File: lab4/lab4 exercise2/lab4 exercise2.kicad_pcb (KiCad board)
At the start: 2 copper layers, 10 parts, among them J1 Conn_01x02_Male, U1 NE555D

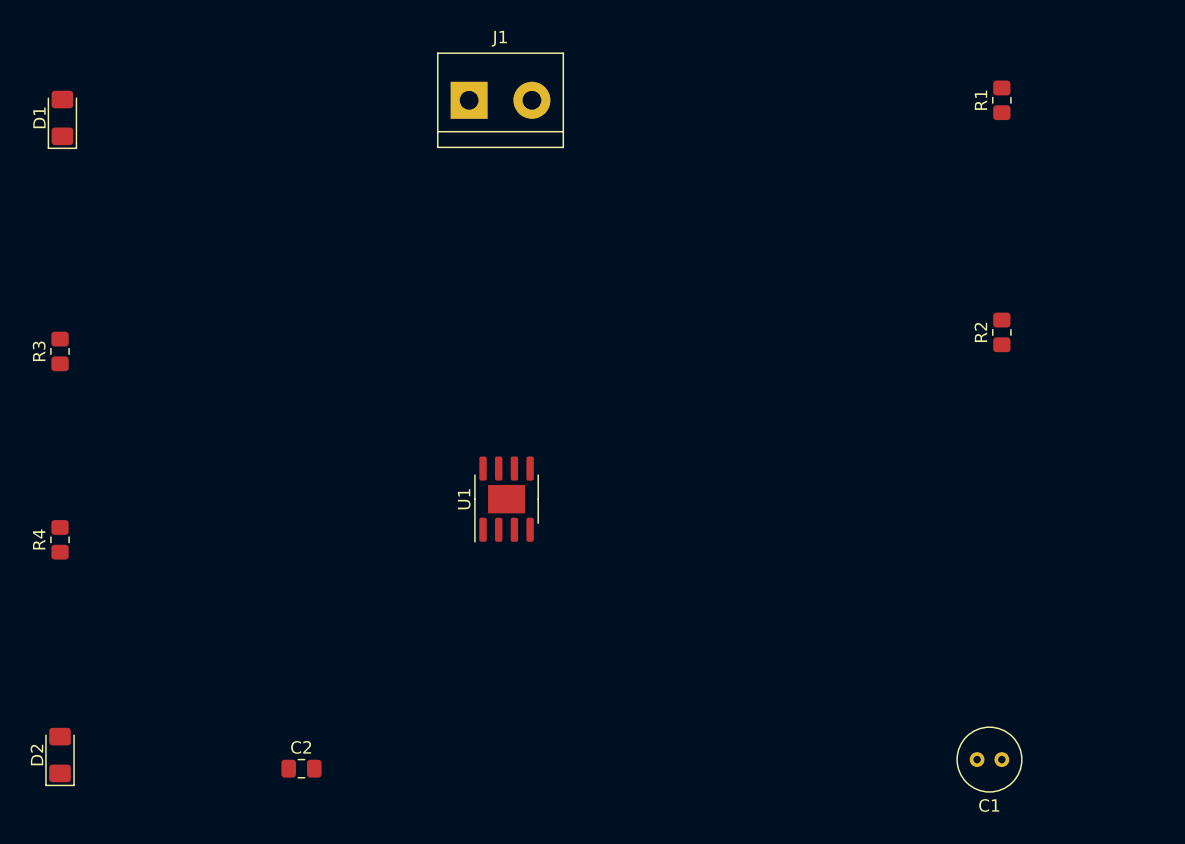
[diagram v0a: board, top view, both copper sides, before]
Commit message: Updated lab 4 pcb layout
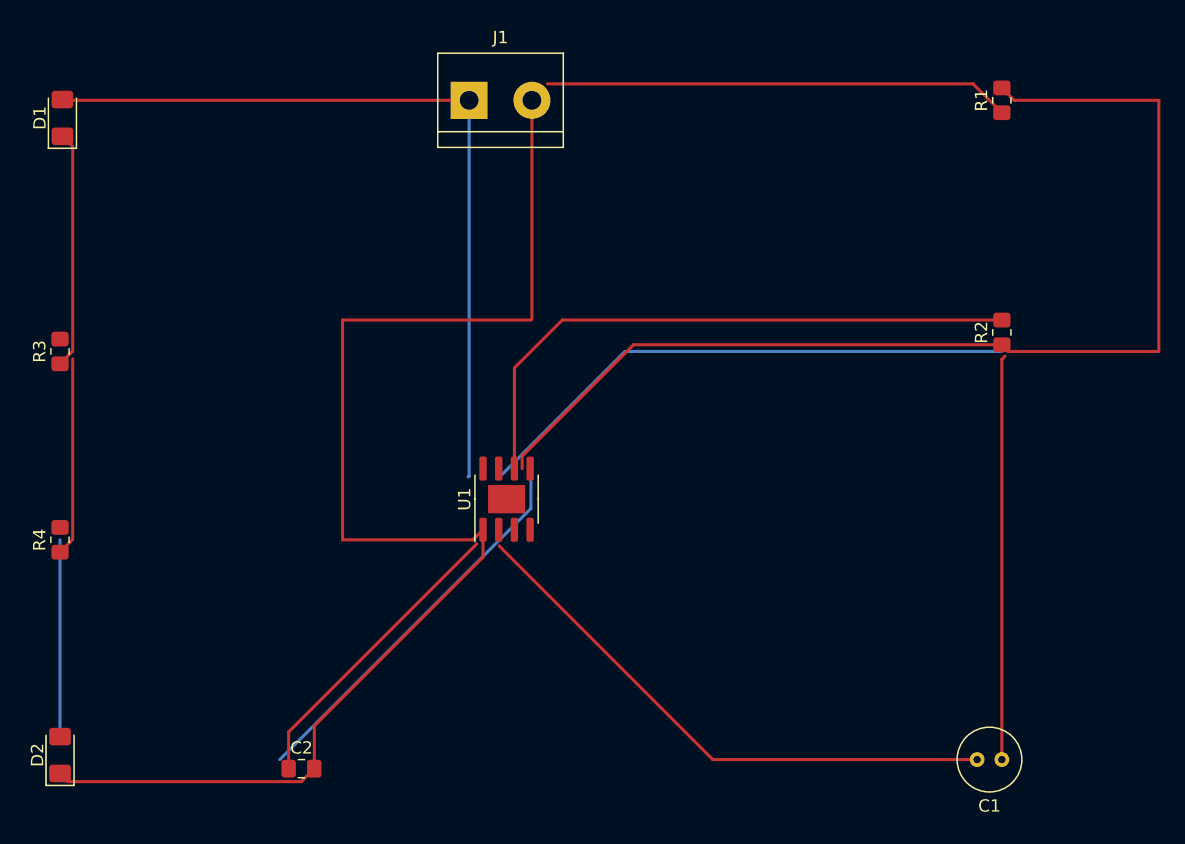
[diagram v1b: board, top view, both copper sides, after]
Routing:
- net GND: track 0.00 -> 154.5 mm
- net +9V: track 0.00 -> 101.2 mm
- net (no net): track 0.00 -> 91.4 mm
- net Net-(R1-Pad2): track 0.00 -> 90.4 mm
- net Net-(C1-Pad1): track 0.00 -> 81.9 mm
- net Net-(C2-Pad1): track 0.00 -> 24.5 mm
- net Net-(D1-Pad1): track 0.00 -> 19.2 mm
- net Net-(R3-Pad2): track 0.00 -> 16.1 mm
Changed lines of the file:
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@@
     )
   )
+  (segment (start 124.46 101.6) (end 104.14 121.92) (width 0.25) (layer "B.Cu") (net 0))
+  (segment (start 86.36 119.38) (end 86.36 104.14) (width 0.25) (layer "B.Cu") (net 0))
+  (segment (start 162.56 88.9) (end 132.08 88.9) (width 0.25) (layer "B.Cu") (net 0))
+  (segment (start 124.46 99.06) (end 124.46 101.6) (width 0.25) (layer "B.Cu") (net 0))
+  (segment (start 132.08 88.9) (end 121.92 99.06) (width 0.25) (layer "B.Cu") (net 0))
+  (segment (start 127 86.36) (end 123.125 90.235) (width 0.25) (layer "F.Cu") (net 1))
+  (segment (start 162.56 89.536396) (end 162.811396 89.285) (width 0.25) (layer "F.Cu") (net 1))
+  (segment (start 162.56 86.36) (end 127 86.36) (width 0.25) (layer "F.Cu") (net 1))
+  (segment (start 162.56 121.92) (end 162.56 89.536396) (width 0.25) (layer "F.Cu") (net 1))
+  (segment (start 123.125 90.235) (end 123.125 98.375) (width 0.25) (layer "F.Cu") (net 1))
+  (segment (start 109.22 86.36) (end 109.22 104.14) (width 0.25) (layer "F.Cu") (net 2))
+  (segment (start 124.54 68.58) (end 124.54 86.28) (width 0.25) (layer "F.Cu") (net 2))
+  (segment (start 105.883744 123.705) (end 106.933744 122.655) (width 0.25) (layer "F.Cu") (net 2))
+  (segment (start 109.22 104.14) (end 119.77 104.14) (width 0.25) (layer "F.Cu") (net 2))
+  (segment (start 120.585 105.548249) (end 120.585 103.325) (width 0.25) (layer "F.Cu") (net 2))
+  (segment (start 106.933744 119.199505) (end 120.585 105.548249) (width 0.25) (layer "F.Cu") (net 2))
+  (segment (start 87.0275 123.705) (end 105.883744 123.705) (width 0.25) (layer "F.Cu") (net 2))
+  (segment (start 160.56 121.92) (end 139.18 121.92) (width 0.25) (layer "F.Cu") (net 2))
+  (segment (start 139.18 121.92) (end 121.885 104.625) (width 0.25) (layer "F.Cu") (net 2))
+  (segment (start 106.933744 122.655) (end 106.933744 119.199505) (width 0.25) (layer "F.Cu") (net 2))
+  (segment (start 119.77 104.14) (end 120.585 103.325) (width 0.25) (layer "F.Cu") (net 2))
+  (segment (start 86.36 123.0375) (end 87.0275 123.705) (width 0.25) (layer "F.Cu") (net 2))
+  (segment (start 124.46 86.36) (end 109.22 86.36) (width 0.25) (layer "F.Cu") (net 2))
+  (segment (start 104.858744 119.687652) (end 120.079823 104.466573) (width 0.25) (layer "F.Cu") (net 3))
+  (segment (start 104.858744 122.655) (end 104.858744 119.687652) (width 0.25) (layer "F.Cu") (net 3))
+  (segment (start 87.385 88.875) (end 86.36 89.9) (width 0.25) (layer "F.Cu") (net 4))
+  (segment (start 86.555 71.4925) (end 87.385 72.3225) (width 0.25) (layer "F.Cu") (net 4))
+  (segment (start 87.385 72.3225) (end 87.385 88.875) (width 0.25) (layer "F.Cu") (net 4))
+  (segment (start 86.555 68.5175) (end 86.6175 68.58) (width 0.25) (layer "F.Cu") (net 5))
+  (segment (start 162.56 69.58) (end 160.22953 67.24953) (width 0.25) (layer "F.Cu") (net 5))
+  (segment (start 86.6175 68.58) (end 119.46 68.58) (width 0.25) (layer "F.Cu") (net 5))
+  (segment (start 160.22953 67.24953) (end 125.79047 67.24953) (width 0.25) (layer "F.Cu") (net 5))
+  (segment (start 119.46 68.58) (end 119.46 98.98) (width 0.25) (layer "B.Cu") (net 5))
+  (segment (start 119.46 98.98) (end 119.38 99.06) (width 0.25) (layer "B.Cu") (net 5))
+  (segment (start 162.56 88.36) (end 162.56 88.9) (width 0.25) (layer "F.Cu") (net 7))
+  (segment (start 175.26 68.58) (end 175.26 88.9) (width 0.25) (layer "F.Cu") (net 7))
+  (segment (start 162.56 67.58) (end 163.56 68.58) (width 0.25) (layer "F.Cu") (net 7))
+  (segment (start 132.763249 88.36) (end 123.75 97.373249) (width 0.25) (layer "F.Cu") (net 7))
+  (segment (start 162.56 88.36) (end 132.763249 88.36) (width 0.25) (layer "F.Cu") (net 7))
+  (segment (start 163.1 88.9) (end 162.56 88.36) (width 0.25) (layer "F.Cu") (net 7))
+  (segment (start 175.26 88.9) (end 163.1 88.9) (width 0.25) (layer "F.Cu") (net 7))
+  (segment (start 163.56 68.58) (end 175.26 68.58) (width 0.25) (layer "F.Cu") (net 7))
+  (segment (start 123.75 97.373249) (end 123.75 98.375) (width 0.25) (layer "F.Cu") (net 7))
+  (segment (start 86.36 105.14) (end 87.385 104.115) (width 0.25) (layer "F.Cu") (net 8))
+  (segment (start 87.385 104.115) (end 87.385 89.511396) (width 0.25) (layer "F.Cu") (net 8))
 )
